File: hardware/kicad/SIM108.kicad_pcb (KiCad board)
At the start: 2 copper layers, 75 x 75 mm, 85 parts, among them J1 Screw_Terminal_01x09, J2 CAN, Q1 BC547, Q10 BC337, Q11 BC547, Q12 BC337, Q13 BC547, Q14 BC337, Q15 BC547, Q16 BC337, Q2 BC337, Q3 BC547, Q4 BC337, Q5 BC547, Q6 BC337, Q7 BC547, Q8 BC337, Q9 BC547, SW1 INSTANCE, SW2 BUS, U1 74HC595, U10 SFH617A-1, U11 SFH617A-1, U12 SFH617A-1, U2 MCP2551-I-P, U3 TMR-1211, U4 Teensy_3.2, U5 SFH617A-1, U6 SFH617A-1, U7 SFH617A-1, U8 SFH617A-1, U9 SFH617A-1

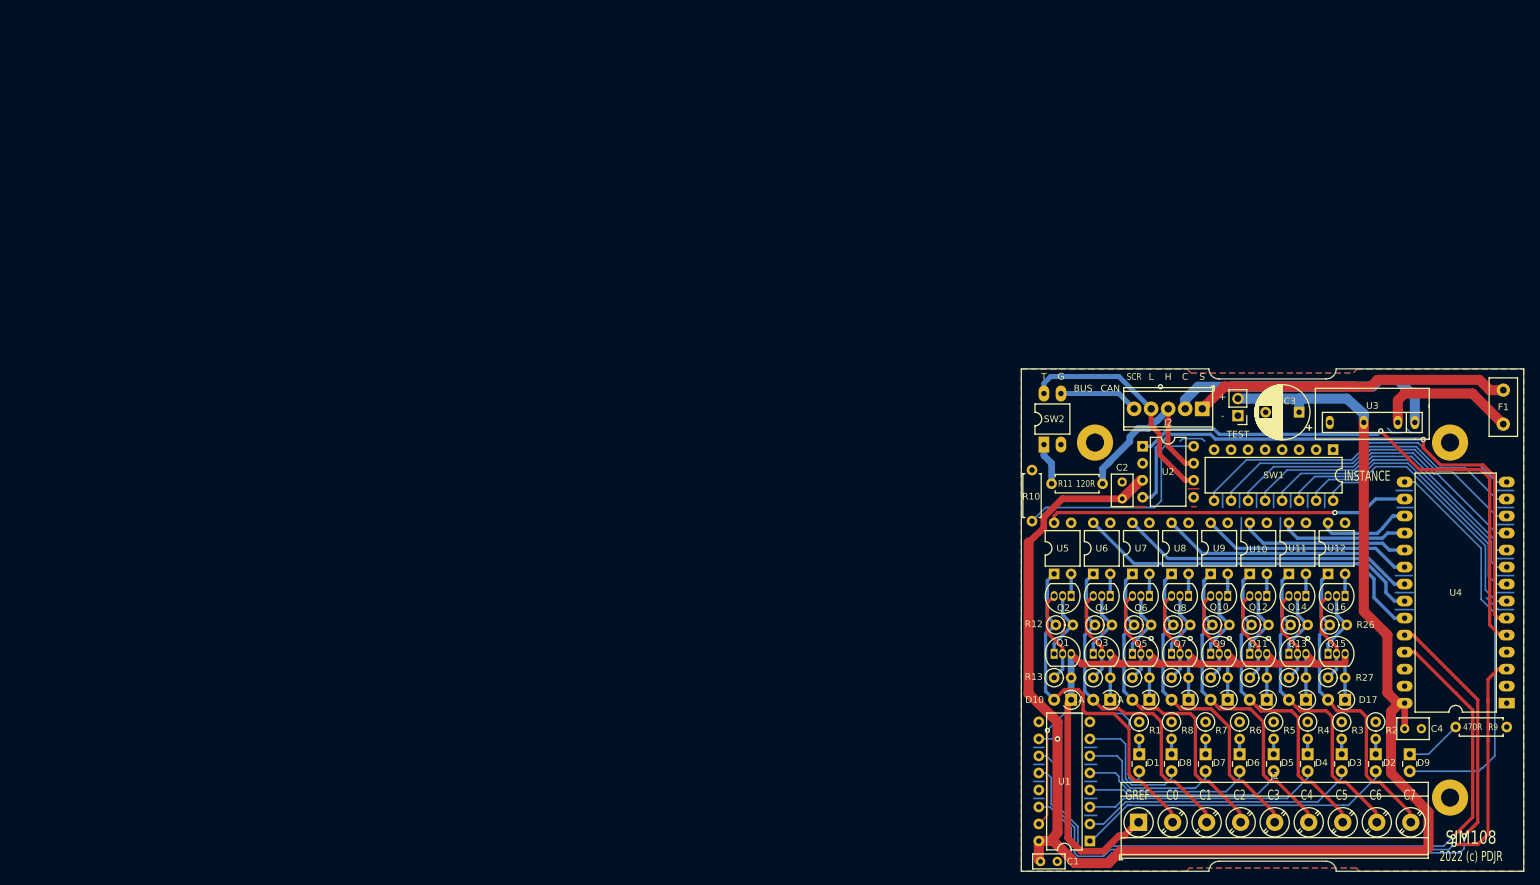
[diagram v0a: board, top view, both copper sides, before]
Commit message: New board size
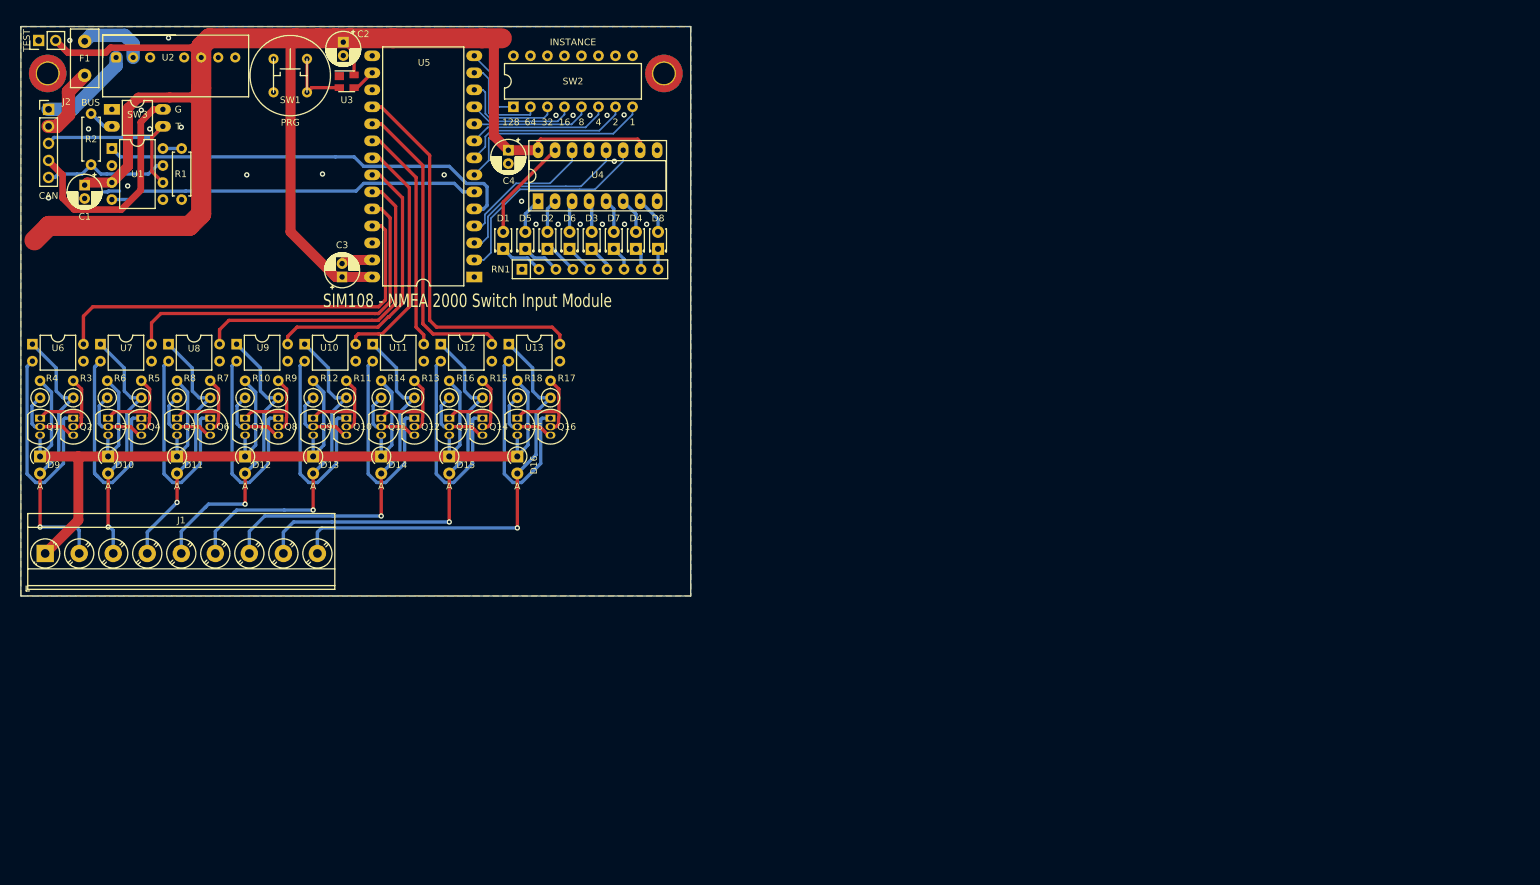
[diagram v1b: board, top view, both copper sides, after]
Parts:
- removed D17: IN4148, Diode_THT:D_A-405_P2.54mm_Vertical_AnodeUp
- removed R19, R21, R23, R25, R27: 100R, Resistor_THT:R_Axial_DIN0207_L6.3mm_D2.5mm_P2.54mm_Vertical
- removed R20, R22, R24, R26: 10K 0.5W, Resistor_THT:R_Axial_DIN0207_L6.3mm_D2.5mm_P2.54mm_Vertical
- removed the REF** at (200.0, 151.0)
- removed the REF** at (147.0, 98.0)
- removed the REF** at (200.0, 98.0)
- removed the U5 at (140.9, 117.6)
- added REF**: MountingHole_3.2mm_M3_DIN965_Pad_TopBottom, MountingHole:MountingHole_3.2mm_M3_DIN965_Pad_TopBottom, F.Cu at (-9.36, 42.9)
- added REF**: MountingHole_3.2mm_M3_DIN965_Pad_TopBottom, MountingHole:MountingHole_3.2mm_M3_DIN965_Pad_TopBottom, F.Cu at (82.6, 42.9)
- added RN1: R_Network08, Resistor_THT:R_Array_SIP9, F.Cu at (61.4, 72.1)
- added SW3: BUS, Package_DIP:DIP-4_W7.62mm_LongPads, F.Cu at (0.23, 48.3)
- added U13: SFH617A-1, Package_DIP:DIP-4_W7.62mm, F.Cu at (59.5, 83.3)
- added U4: 74HC595, Package_DIP:DIP-16_W7.62mm_Socket_LongPads, F.Cu at (63.9, 62.0)
- C1: footprint Capacitor_THT:C_Rect_L4.6mm_W2.0mm_P2.50mm_MKS02_FKP02 -> Capacitor_THT:CP_Radial_D5.0mm_P2.00mm
- C2: value 100n -> 100nF; footprint Capacitor_THT:C_Rect_L4.6mm_W3.0mm_P2.50mm_MKS02_FKP02 -> Capacitor_THT:CP_Radial_D5.0mm_P2.00mm
- C3: value 1000uF -> 100nF; footprint Capacitor_THT:CP_Radial_D8.0mm_P5.00mm -> Capacitor_THT:CP_Radial_D5.0mm_P2.00mm
- C4: footprint Capacitor_THT:C_Rect_L4.6mm_W3.0mm_P2.50mm_MKS02_FKP02 -> Capacitor_THT:CP_Radial_D5.0mm_P2.00mm
- D1, D2, D3, D4, D5, D6, D7, D8: value LED_Small -> LED; footprint LED_THT:LED_Rectangular_W3.0mm_H2.0mm -> LED_THT:LED_D1.8mm_W3.3mm_H2.4mm
- D9: value LED_Small -> IN4148; footprint LED_THT:LED_Rectangular_W3.0mm_H2.0mm -> Diode_THT:D_A-405_P2.54mm_Vertical_AnodeUp
- J2: footprint TerminalBlock_Phoenix:TerminalBlock_Phoenix_MPT-0,5-5-2.54_1x05_P2.54mm_Horizontal -> Connector_PinHeader_2.54mm:PinHeader_1x05_P2.54mm_Vertical
- R1: value 470R -> 4K7; footprint Resistor_THT:R_Axial_DIN0207_L6.3mm_D2.5mm_P2.54mm_Vertical -> Resistor_THT:R_Axial_DIN0207_L6.3mm_D2.5mm_P7.62mm_Horizontal
- R10: value 4K7 -> 100R; footprint Resistor_THT:R_Axial_DIN0207_L6.3mm_D2.5mm_P7.62mm_Horizontal -> Resistor_THT:R_Axial_DIN0207_L6.3mm_D2.5mm_P2.54mm_Vertical
- R11: value 120R -> 10K 0.5W; footprint Resistor_THT:R_Axial_DIN0207_L6.3mm_D2.5mm_P7.62mm_Horizontal -> Resistor_THT:R_Axial_DIN0207_L6.3mm_D2.5mm_P2.54mm_Vertical
- R12, R14, R16, R18: value 10K 0.5W -> 100R
- R13, R15, R17: value 100R -> 10K 0.5W
- R2: value 470R -> 120R; footprint Resistor_THT:R_Axial_DIN0207_L6.3mm_D2.5mm_P2.54mm_Vertical -> Resistor_THT:R_Axial_DIN0207_L6.3mm_D2.5mm_P7.62mm_Horizontal
- R3, R5, R7: value 470R -> 10K 0.5W
- R4, R6, R8: value 470R -> 100R
- R9: value 470R -> 10K 0.5W; footprint Resistor_THT:R_Axial_DIN0207_L6.3mm_D2.5mm_P7.62mm_Horizontal -> Resistor_THT:R_Axial_DIN0207_L6.3mm_D2.5mm_P2.54mm_Vertical
- SW1: value INSTANCE -> PRG; footprint Package_DIP:DIP-16_W7.62mm -> PDJR-connectors:PCB_PUSH_BUTTON
- SW2: value BUS -> INSTANCE; footprint Package_DIP:DIP-4_W7.62mm_LongPads -> Package_DIP:DIP-16_W7.62mm
- U1: value 74HC595 -> MCP2551-I-P; footprint Package_DIP:DIP-16_W7.62mm -> Package_DIP:DIP-8_W7.62mm
- U2: value MCP2551-I-P -> TMR_2411; footprint Package_DIP:DIP-8_W7.62mm -> PDJR-connectors:TMR_2411
- U3: value TMR-1211 -> MAX6816; footprint PDJR-connectors:TMR-1-1211 -> Package_TO_SOT_SMD:SOT-143
- moved F1 216.9 mm to (-3.83, 43.2), turned to 90 degrees
- moved D9 209.2 mm to (-10.5, 100.1)
- moved R2 209.0 mm to (-2.87, 56.5), turned to 90 degrees
- moved R3 195.4 mm to (-5.54, 91.3), turned to 90 degrees
- moved R4 195.3 mm to (-10.5, 91.3), turned to 90 degrees
- moved TEST 187.6 mm to (-10.7, 38.0), turned to 90 degrees
- moved R9 182.5 mm to (25.1, 91.3), turned to 90 degrees
- moved U1 178.9 mm to (0.23, 54.1), turned to 0 degrees
- moved J2 177.9 mm to (-9.22, 48.3), turned to 0 degrees
- moved R5 175.8 mm to (4.62, 91.3), turned to 90 degrees
- moved R6 175.8 mm to (-0.46, 91.3), turned to 90 degrees
- moved C1 174.8 mm to (-3.83, 59.6), turned to 270 degrees
- moved J1 168.1 mm to (-9.73, 114.6)
- moved SW1 166.9 mm to (24.4, 45.7), turned to 0 degrees
- moved U5 166.7 mm to (54.3, 73.3)
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- renumbered U4 to U5
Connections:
- D10 pad 2: /SPST_CH0 -> /SPST_CH1
- D11 pad 2: /SPST_CH1 -> /SPST_CH2
- D12 pad 2: /SPST_CH2 -> /SPST_CH3
- D13 pad 2: /SPST_CH3 -> /SPST_CH4
- D14 pad 2: /SPST_CH4 -> /SPST_CH5
- D15 pad 2: /SPST_CH5 -> /SPST_CH6
- D16 pad 2: /SPST_CH6 -> /SPST_CH7
- D9 pad 1: Net-(D9-Pad1) -> /SPST_GND
- D9 pad 2: /LED_PWR -> /SPST_CH0
- F1 pad 1: /NET_S -> Net-(F1-Pad1)
- J2 pad 1: /NET_S -> /NET_C
- J2 pad 2: /NET_C -> Net-(F1-Pad1)
- J2 pad 3: /CAN_H -> /CAN_L
- J2 pad 4: /CAN_L -> /CAN_SCR
- J2 pad 5: /CAN_SCR -> /CAN_H
- R1 pad 2: Net-(D1-Pad1) -> Net-(R1-Pad2)
- R10 pad 1: GND -> Net-(Q7-Pad2)
- R10 pad 2: Net-(R10-Pad2) -> /SPST_GND
- R11 pad 1: /CAN_H -> /SPST_CH4
- R11 pad 2: /TERM_A -> Net-(Q10-Pad2)
- R12 pad 1: /SPST_CH0 -> Net-(Q10-Pad3)
- R12 pad 2: Net-(Q1-Pad1) -> /SPST_GND
- R13 pad 1: Net-(Q1-Pad2) -> /SPST_CH5
- R13 pad 2: /SPST_GND -> Net-(Q11-Pad1)
- R14 pad 1: /SPST_CH1 -> Net-(Q11-Pad2)
- R14 pad 2: Net-(Q3-Pad1) -> /SPST_GND
- R15 pad 1: Net-(Q3-Pad2) -> /SPST_CH6
- R15 pad 2: /SPST_GND -> Net-(Q13-Pad1)
- R16 pad 1: /SPST_CH2 -> Net-(Q13-Pad2)
- R16 pad 2: Net-(Q5-Pad1) -> /SPST_GND
- R17 pad 1: Net-(Q5-Pad2) -> /SPST_CH7
- R17 pad 2: /SPST_GND -> Net-(Q15-Pad1)
- R18 pad 1: /SPST_CH3 -> Net-(Q15-Pad2)
- R18 pad 2: Net-(Q7-Pad1) -> /SPST_GND
- R2 pad 1: GND -> /CAN_H
- R2 pad 2: Net-(D2-Pad1) -> /TERM_A
- R3 pad 1: GND -> /SPST_CH0
- R3 pad 2: Net-(D3-Pad1) -> Net-(Q1-Pad1)
- R4 pad 1: GND -> Net-(Q1-Pad2)
- R4 pad 2: Net-(D4-Pad1) -> /SPST_GND
- R5 pad 1: GND -> /SPST_CH1
- R5 pad 2: Net-(D5-Pad1) -> Net-(Q3-Pad1)
- R6 pad 1: GND -> Net-(Q3-Pad2)
- R6 pad 2: Net-(D6-Pad1) -> /SPST_GND
- R7 pad 1: GND -> /SPST_CH2
- R7 pad 2: Net-(D7-Pad1) -> Net-(Q5-Pad1)
- R8 pad 1: GND -> Net-(Q5-Pad2)
- R8 pad 2: Net-(D8-Pad1) -> /SPST_GND
- R9 pad 1: Net-(D9-Pad1) -> /SPST_CH3
- R9 pad 2: GND -> Net-(Q7-Pad1)
- SW1 pad 2: GND -> Net-(SW1-Pad2)
- SW2 pad 1: /TERM_A -> /ADDR_0
- SW2 pad 2: GND -> /ADDR_1
- SW2 pad 3: /CAN_SCR -> /ADDR_2
- SW2 pad 4: /CAN_L -> /ADDR_3
- U1 pad 1: Net-(D2-Pad2) -> /CAN_TX
- U1 pad 2: Net-(D3-Pad2) -> GND
- U1 pad 3: Net-(D4-Pad2) -> +5V
- U1 pad 4: Net-(D5-Pad2) -> /CAN_RX
- U1 pad 5: Net-(D6-Pad2) -> Net-(U1-Pad5)
- U1 pad 6: Net-(D7-Pad2) -> /CAN_L
- U1 pad 7: Net-(D8-Pad2) -> /CAN_H
- U1 pad 8: GND -> Net-(R1-Pad2)
- U10 pad 1: /SPST_CH5 -> /SPST_CH4
- U10 pad 2: Net-(Q12-Pad1) -> Net-(Q10-Pad1)
- U10 pad 4: /CH5 -> /CH4
- U11 pad 1: /SPST_CH6 -> /SPST_CH5
- U11 pad 2: Net-(Q14-Pad1) -> Net-(Q12-Pad1)
- U11 pad 4: /CH6 -> /CH5
- U12 pad 1: /SPST_CH7 -> /SPST_CH6
- U12 pad 2: Net-(Q16-Pad1) -> Net-(Q14-Pad1)
- U12 pad 4: /CH7 -> /CH6
- U2 pad 1: /CAN_TX -> /NET_C
- U2 pad 2: GND -> Net-(F1-Pad2)
- U2 pad 3: +5V -> (no net)
- U2 pad 5: Net-(U2-Pad5) -> (no net)
- U2 pad 6: /CAN_L -> +5V
- U2 pad 7: /CAN_H -> GND
- U2 pad 8: Net-(R10-Pad2) -> (no net)
- U3 pad 1: /NET_C -> GND
- U3 pad 2: Net-(F1-Pad2) -> Net-(SW1-Pad2)
- U5 pad 10: /ADDR_3 -> /ADDR_4
- U5 pad 11: /ADDR_4 -> /ADDR_3
- U5 pad 12: /ADDR_5 -> /ADDR_2
- U5 pad 13: /ADDR_6 -> /ADDR_1
- U5 pad 14: /ADDR_7 -> /ADDR_0
- U5 pad 15: /LED_PWR -> Net-(U5-Pad15)
- U5 pad 16: /CH0 -> /PRG
- U5 pad 17: /CH7 -> Net-(U5-Pad17)
- U5 pad 18: /CH6 -> /CH7
- U5 pad 19: /CH5 -> /CH6
- U5 pad 2: Net-(U4-Pad2) -> /MPX_CLOCK
- U5 pad 20: /CH4 -> /CH5
- U5 pad 21: /CH3 -> /CH4
- U5 pad 22: /CH2 -> /CH3
- U5 pad 23: /CH1 -> /CH2
- U5 pad 24: /DATA -> /CH1
- U5 pad 25: /CLOCK -> /CH0
- U5 pad 3: /LATCH -> /MPX_LATCH
- U5 pad 4: Net-(U4-Pad4) -> /MPX_DATA
- U5 pad 7: /ADDR_0 -> /ADDR_7
- U5 pad 8: /ADDR_1 -> /ADDR_6
- U5 pad 9: /ADDR_2 -> /ADDR_5
- U6 pad 1: /SPST_CH1 -> /SPST_CH0
- U6 pad 2: Net-(Q4-Pad1) -> Net-(Q2-Pad1)
- U6 pad 4: /CH1 -> /CH0
- U7 pad 1: /SPST_CH2 -> /SPST_CH1
- U7 pad 2: Net-(Q6-Pad1) -> Net-(Q4-Pad1)
- U7 pad 4: /CH2 -> /CH1
- U8 pad 1: /SPST_CH3 -> /SPST_CH2
- U8 pad 2: Net-(Q8-Pad1) -> Net-(Q6-Pad1)
- U8 pad 4: /CH3 -> /CH2
- U9 pad 1: /SPST_CH4 -> /SPST_CH3
- U9 pad 2: Net-(Q10-Pad1) -> Net-(Q8-Pad1)
- U9 pad 4: /CH4 -> /CH3
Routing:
- net /CLOCK: track 108.3 -> 0.00 mm, vias 1 -> 0
- net /DATA: track 107.7 -> 0.00 mm, vias 1 -> 0
- net /LATCH: track 105.2 -> 0.00 mm, vias 1 -> 0
- net GND: track 98.9 -> 7.06 mm, vias 6 -> 24
- net /SPST_GND: track 144.6 -> 214.3 mm
- net /LED_PWR: track 61.0 -> 0.00 mm
- net /NET_S: track 47.4 -> 0.00 mm
- net /CH7: track 13.9 -> 57.9 mm
- net Net-(D2-Pad2): track 47.8 -> 5.05 mm
- net Net-(D3-Pad2): track 41.4 -> 4.73 mm
- net Net-(R10-Pad2): track 33.5 -> 0.00 mm
- net /MPX_CLOCK: track 0.00 -> 33.0 mm
- net Net-(Q4-Pad1): track 3.30 -> 34.1 mm
- net /CAN_RX: track 86.3 -> 55.6 mm, vias 1 -> 0
- net /ADDR_0: track 40.9 -> 11.3 mm
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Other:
- board size 75 x 75 mm -> 100 x 85 mm
- board text added: "1"
- board text added: "128"
- board text added: "16"
- board text added: "2"
- board text added: "32"
- board text added: "4"
- board text added: "64"
- board text added: "8"
- board text added: "SIM108 - NMEA 2000 Switch Input Module"
- board text removed: "+"
- board text removed: "-"
- board text removed: "2022 (c) PDJR"
- board text removed: "C"
- board text removed: "C0"
- board text removed: "C1"
- board text removed: "C2"
- board text removed: "C3"
- board text removed: "C4"
- board text removed: "C5"
- board text removed: "C6"
- board text removed: "C7"
- board text removed: "GREF"
- board text removed: "H"
- board text removed: "L"
- board text removed: "S"
- board text removed: "SCR"
- board text removed: "SIM108"

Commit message: PCB tweaks
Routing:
- net /CH7: track 57.9 -> 63.5 mm
- net /CH6: track 45.8 -> 50.6 mm
- net /CH5: track 34.2 -> 38.7 mm
- net /CH3: track 42.0 -> 45.3 mm
- net /CH2: track 48.9 -> 51.3 mm
- net /CH4: track 36.1 -> 38.0 mm
- net GND: vias 24 -> 28

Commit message: Stuff
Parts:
- added R19: 10K, Resistor_THT:R_Axial_DIN0207_L6.3mm_D2.5mm_P2.54mm_Vertical, F.Cu at (-4.65, 77.2)
- added R20: 10K, Resistor_THT:R_Axial_DIN0207_L6.3mm_D2.5mm_P2.54mm_Vertical, F.Cu at (113.2, 57.3)
- added R21: 10K, Resistor_THT:R_Axial_DIN0207_L6.3mm_D2.5mm_P2.54mm_Vertical, F.Cu at (128.5, 47.3)
- added R22: 10K, Resistor_THT:R_Axial_DIN0207_L6.3mm_D2.5mm_P2.54mm_Vertical, F.Cu at (97.9, 47.3)
- added R23: 10K, Resistor_THT:R_Axial_DIN0207_L6.3mm_D2.5mm_P2.54mm_Vertical, F.Cu at (113.2, 47.3)
- added R24: 10K, Resistor_THT:R_Axial_DIN0207_L6.3mm_D2.5mm_P2.54mm_Vertical, F.Cu at (128.5, 37.3)
- added R25: 10K, Resistor_THT:R_Axial_DIN0207_L6.3mm_D2.5mm_P2.54mm_Vertical, F.Cu at (97.9, 37.3)
- added R26: 10K, Resistor_THT:R_Axial_DIN0207_L6.3mm_D2.5mm_P2.54mm_Vertical, F.Cu at (97.9, 57.3)
- added U14: MAX6816, Package_TO_SOT_SMD:SOT-143, F.Cu at (-10.5, 77.0)
- added U15: MAX6816, Package_TO_SOT_SMD:SOT-143, F.Cu at (119.9, 57.5)
- added U16: MAX6816, Package_TO_SOT_SMD:SOT-143, F.Cu at (135.2, 47.5)
- added U17: MAX6816, Package_TO_SOT_SMD:SOT-143, F.Cu at (104.6, 47.5)
- added U18: MAX6816, Package_TO_SOT_SMD:SOT-143, F.Cu at (119.9, 47.5)
- added U19: MAX6816, Package_TO_SOT_SMD:SOT-143, F.Cu at (135.2, 37.6)
- added U20: MAX6816, Package_TO_SOT_SMD:SOT-143, F.Cu at (104.6, 37.6)
- added U21: MAX6816, Package_TO_SOT_SMD:SOT-143, F.Cu at (104.6, 57.5)
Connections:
- D10 pad 1: /SPST_GND -> GND
- D11 pad 1: /SPST_GND -> GND
- D12 pad 1: /SPST_GND -> GND
- D13 pad 1: /SPST_GND -> GND
- D14 pad 1: /SPST_GND -> GND
- D15 pad 1: /SPST_GND -> GND
- D16 pad 1: /SPST_GND -> GND
- D9 pad 1: /SPST_GND -> GND
- J1 pad 1: /SPST_GND -> GND
- Q1 pad 3: /SPST_GND -> GND
- Q11 pad 3: /SPST_GND -> GND
- Q13 pad 3: /SPST_GND -> GND
- Q15 pad 3: /SPST_GND -> GND
- Q3 pad 3: /SPST_GND -> GND
- Q5 pad 3: /SPST_GND -> GND
- Q7 pad 3: /SPST_GND -> GND
- Q9 pad 3: /SPST_GND -> GND
- R10 pad 2: /SPST_GND -> GND
- R12 pad 2: /SPST_GND -> GND
- R14 pad 2: /SPST_GND -> GND
- R16 pad 2: /SPST_GND -> GND
- R18 pad 2: /SPST_GND -> GND
- R4 pad 2: /SPST_GND -> GND
- R6 pad 2: /SPST_GND -> GND
- R8 pad 2: /SPST_GND -> GND
- U10 pad 3: GND -> Net-(R23-Pad1)
- U10 pad 4: /CH4 -> /OOI_04/OII_OUT_VCC
- U11 pad 3: GND -> Net-(R24-Pad1)
- U11 pad 4: /CH5 -> /OOI_05/OII_OUT_VCC
- U12 pad 3: GND -> Net-(R25-Pad1)
- U12 pad 4: /CH6 -> /OOI_06/OII_OUT_VCC
- U13 pad 3: GND -> Net-(R26-Pad1)
- U13 pad 4: /CH7 -> /OII_07/OII_OUT_VCC
- U5 pad 18: /CH7 -> /CH0
- U5 pad 25: /CH0 -> /CH7
- U6 pad 3: GND -> Net-(R19-Pad1)
- U6 pad 4: /CH0 -> +5V
- U7 pad 3: GND -> Net-(R20-Pad1)
- U7 pad 4: /CH1 -> /OII_01/OII_OUT_VCC
- U8 pad 3: GND -> Net-(R21-Pad1)
- U8 pad 4: /CH2 -> /OII_02/OII_OUT_VCC
- U9 pad 3: GND -> Net-(R22-Pad1)
- U9 pad 4: /CH3 -> /OOI_03/OII_OUT_VCC
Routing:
- net /SPST_GND: track 214.3 -> 0.00 mm
- net GND: track 7.06 -> 221.4 mm, vias 28 -> 22
- net /CH7: track 63.5 -> 0.00 mm
- net /CH1: track 55.9 -> 0.00 mm
- net /CH2: track 51.3 -> 0.00 mm
- net /CH3: track 45.3 -> 1.09 mm
- net /CH4: track 38.0 -> 0.00 mm
- net /CH6: track 50.6 -> 20.2 mm
- net +5V: track 244.4 -> 266.3 mm
- net /OII_07/OII_OUT_VCC: track 0.00 -> 21.7 mm
- net /CH5: track 38.7 -> 20.2 mm
- net Net-(R19-Pad1): track 0.00 -> 14.8 mm
- net /OOI_06/OII_OUT_VCC: track 0.00 -> 12.1 mm
- net /CH0: track 62.9 -> 73.3 mm
- net /OOI_05/OII_OUT_VCC: track 0.00 -> 3.01 mm

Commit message: Debounce
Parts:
- moved U16 131.0 mm to (10.1, 86.1), turned to 180 degrees
- moved U15 123.3 mm to (-0.08, 86.1), turned to 180 degrees
- moved R21 119.2 mm to (15.9, 86.4), turned to 180 degrees
- moved R20 111.3 mm to (5.77, 86.4), turned to 180 degrees
- moved U19 106.4 mm to (40.6, 86.1), turned to 180 degrees
- moved U18 97.4 mm to (30.4, 86.1), turned to 180 degrees
- moved R24 95.7 mm to (46.4, 86.4), turned to 180 degrees
- moved U17 92.7 mm to (20.2, 86.1), turned to 180 degrees
- moved R23 86.3 mm to (36.2, 86.4), turned to 180 degrees
- moved R22 81.7 mm to (26.1, 86.4), turned to 180 degrees
- moved U20 72.5 mm to (50.7, 86.1), turned to 180 degrees
- moved R25 64.1 mm to (56.6, 86.4), turned to 180 degrees
- moved U21 52.2 mm to (60.9, 86.1), turned to 180 degrees
- moved R26 42.6 mm to (66.7, 86.4), turned to 180 degrees
- moved R19 9.15 mm to (-4.39, 86.4)
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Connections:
- D10 pad 1: GND -> /SPST_GND
- D11 pad 1: GND -> /SPST_GND
- D12 pad 1: GND -> /SPST_GND
- D13 pad 1: GND -> /SPST_GND
- D14 pad 1: GND -> /SPST_GND
- D15 pad 1: GND -> /SPST_GND
- D16 pad 1: GND -> /SPST_GND
- D9 pad 1: GND -> /SPST_GND
- J1 pad 1: GND -> /SPST_GND
- Q1 pad 3: GND -> /SPST_GND
- Q11 pad 3: GND -> /SPST_GND
- Q13 pad 3: GND -> /SPST_GND
- Q15 pad 3: GND -> /SPST_GND
- Q3 pad 3: GND -> /SPST_GND
- Q5 pad 3: GND -> /SPST_GND
- Q7 pad 3: GND -> /SPST_GND
- Q9 pad 3: GND -> /SPST_GND
- R10 pad 2: GND -> /SPST_GND
- R12 pad 2: GND -> /SPST_GND
- R14 pad 2: GND -> /SPST_GND
- R16 pad 2: GND -> /SPST_GND
- R18 pad 2: GND -> /SPST_GND
- R19 pad 1: Net-(R19-Pad1) -> +5V
- R19 pad 2: GND -> Net-(R19-Pad2)
- R20 pad 1: Net-(R20-Pad1) -> +5V
- R20 pad 2: GND -> Net-(R20-Pad2)
- R21 pad 1: Net-(R21-Pad1) -> +5V
- R21 pad 2: GND -> Net-(R21-Pad2)
- R22 pad 1: Net-(R22-Pad1) -> +5V
- R22 pad 2: GND -> Net-(R22-Pad2)
- R23 pad 1: Net-(R23-Pad1) -> +5V
- R23 pad 2: GND -> Net-(R23-Pad2)
- R24 pad 1: Net-(R24-Pad1) -> +5V
- R24 pad 2: GND -> Net-(R24-Pad2)
- R25 pad 1: Net-(R25-Pad1) -> +5V
- R25 pad 2: GND -> Net-(R25-Pad2)
- R26 pad 1: Net-(R26-Pad1) -> +5V
- R26 pad 2: GND -> Net-(R26-Pad2)
- R4 pad 2: GND -> /SPST_GND
- R6 pad 2: GND -> /SPST_GND
- R8 pad 2: GND -> /SPST_GND
- U10 pad 3: Net-(R23-Pad1) -> GND
- U10 pad 4: /OOI_04/OII_OUT_VCC -> Net-(R23-Pad2)
- U11 pad 3: Net-(R24-Pad1) -> GND
- U11 pad 4: /OOI_05/OII_OUT_VCC -> Net-(R24-Pad2)
- U12 pad 3: Net-(R25-Pad1) -> GND
- U12 pad 4: /OOI_06/OII_OUT_VCC -> Net-(R25-Pad2)
- U13 pad 3: Net-(R26-Pad1) -> GND
- U13 pad 4: /OII_07/OII_OUT_VCC -> Net-(R26-Pad2)
- U14 pad 2: Net-(R19-Pad1) -> Net-(R19-Pad2)
- U15 pad 2: Net-(R20-Pad1) -> Net-(R20-Pad2)
- U15 pad 4: /OII_01/OII_OUT_VCC -> +5V
- U16 pad 2: Net-(R21-Pad1) -> Net-(R21-Pad2)
- U16 pad 4: /OII_02/OII_OUT_VCC -> +5V
- U17 pad 2: Net-(R22-Pad1) -> Net-(R22-Pad2)
- U17 pad 4: /OOI_03/OII_OUT_VCC -> +5V
- U18 pad 2: Net-(R23-Pad1) -> Net-(R23-Pad2)
- U18 pad 4: /OOI_04/OII_OUT_VCC -> +5V
- U19 pad 2: Net-(R24-Pad1) -> Net-(R24-Pad2)
- U19 pad 4: /OOI_05/OII_OUT_VCC -> +5V
- U20 pad 2: Net-(R25-Pad1) -> Net-(R25-Pad2)
- U20 pad 4: /OOI_06/OII_OUT_VCC -> +5V
- U21 pad 2: Net-(R26-Pad1) -> Net-(R26-Pad2)
- U21 pad 4: /OII_07/OII_OUT_VCC -> +5V
- U5 pad 19: /CH6 -> /CH1
- U5 pad 20: /CH5 -> /CH2
- U5 pad 21: /CH4 -> /CH3
- U5 pad 22: /CH3 -> /CH4
- U5 pad 23: /CH2 -> /CH5
- U5 pad 24: /CH1 -> /CH7
- U5 pad 25: /CH7 -> /CH6
- U6 pad 3: Net-(R19-Pad1) -> GND
- U6 pad 4: +5V -> Net-(R19-Pad2)
- U7 pad 3: Net-(R20-Pad1) -> GND
- U7 pad 4: /OII_01/OII_OUT_VCC -> Net-(R20-Pad2)
- U8 pad 3: Net-(R21-Pad1) -> GND
- U8 pad 4: /OII_02/OII_OUT_VCC -> Net-(R21-Pad2)
- U9 pad 3: Net-(R22-Pad1) -> GND
- U9 pad 4: /OOI_03/OII_OUT_VCC -> Net-(R22-Pad2)
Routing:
- net /SPST_GND: track 0.00 -> 323.3 mm
- net GND: track 221.4 -> 7.06 mm, vias 22 -> 38
- net +5V: track 266.3 -> 369.1 mm
- net /CH1: track 0.00 -> 88.5 mm, vias 0 -> 2
- net /CH2: track 0.00 -> 74.1 mm, vias 0 -> 2
- net /CH3: track 1.09 -> 59.7 mm, vias 0 -> 2
- net /CH4: track 0.00 -> 46.2 mm, vias 0 -> 2
- net /CH7: track 0.00 -> 43.8 mm, vias 0 -> 2
- net /CH0: track 73.3 -> 102.9 mm, vias 0 -> 2
- net /OII_07/OII_OUT_VCC: track 21.7 -> 0.00 mm
- net Net-(R19-Pad1): track 14.8 -> 0.00 mm
- net /OOI_06/OII_OUT_VCC: track 12.1 -> 0.00 mm
- net /CH6: track 20.2 -> 32.2 mm, vias 0 -> 2
- net /CH5: track 20.2 -> 31.2 mm, vias 0 -> 2
- net Net-(R25-Pad2): track 0.00 -> 7.09 mm
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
